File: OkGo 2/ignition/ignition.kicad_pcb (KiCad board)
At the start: 2 copper layers, 94 parts, among them K201 16A SPST, K202 16A SPST, K203 16A SPST, K204 16A SPST, K205 16A SPST, P105 BATT, P106 SMA, P107 ARM_LED, P201 CH3_LED, P203 CH3, P204 CH1_LED, P206 CH1, P207 CH4_LED, P209 CH4, P210 CH2_LED, P212 CH2, Q201 BSS138BK, Q202 BSS138BK, Q203 BSS138BK, Q204 BSS138BK, Q205 BSS138BK, U103 SWD, U105 RFM95W, U106 STM32F071CBT6, U107 TSR 0.5-2433, Y101 8MHz

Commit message: ignition; first attempt at placement
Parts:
- added REF**: hammond1555t2gy, ignition:hammond1555t2gy, F.Cu at (121.9, 101.0)
- added REF**: zippycompact-3s-5_8Ah, ignition:zippycompact-3s-5_8Ah-vert, F.Cu at (122.6, 120.0)
- P107, P201, P204, P207, P210: footprint common:JST-PA-2 -> ignition:JST-PA-2-VERT
- moved U107 221.8 mm to (48.3, 100.1), turned to 180 degrees
- moved R102 217.6 mm to (45.7, 79.2)
- moved R101 217.4 mm to (43.2, 79.2)
- moved TP101 208.6 mm to (43.2, 75.7)
- moved TP102 202.8 mm to (45.7, 75.7)
- moved R220 192.4 mm to (188.0, 76.2), turned to 180 degrees
- moved R218 191.2 mm to (188.0, 73.7), turned to 0 degrees
- moved Q204 189.9 mm to (188.0, 70.6), turned to 0 degrees
- moved D213 188.3 mm to (188.0, 67.1), turned to 0 degrees
- moved R216 179.9 mm to (193.5, 70.1)
- moved D212 178.1 mm to (193.5, 67.1), turned to 0 degrees
- moved R217 176.4 mm to (193.5, 72.6), turned to 0 degrees
- moved F101 172.5 mm to (76.7, 98.6), turned to 180 degrees
- moved TP206 170.2 mm to (193.5, 76.2)
- moved P207 167.4 mm to (166.6, 87.6)
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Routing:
- net /firing/FIRING_DIST: track 0.00 -> 84.6 mm
- net +BATT: track 0.00 -> 66.9 mm
- net Net-(D206-Pad1): track 0.00 -> 19.9 mm
- net Net-(D218-Pad1): track 0.00 -> 19.7 mm
- net Net-(D214-Pad1): track 0.00 -> 18.6 mm
- net Net-(D210-Pad1): track 0.00 -> 17.8 mm
- net Net-(D101-Pad1): track 0.00 -> 16.0 mm
- net (no net): track 0.00 -> 1.90 mm
- added copper zone on B.Cu, net GND
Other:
- board text removed: "ch1"
- board text removed: "ch2"
- board text removed: "ch3"
- board text removed: "ch4"
- board text removed: "upstream"

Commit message: ignition test routing somewhat done
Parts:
- moved TP104 60.7 mm to (49.3, 85.3)
- moved P107 11.2 mm to (46.0, 77.1)
- moved R103 11.2 mm to (50.5, 77.0)
- moved R101 9.71 mm to (44.2, 88.9)
- moved R102 9.71 mm to (46.7, 88.9)
- moved TP101 9.71 mm to (44.2, 85.3)
- moved TP102 9.71 mm to (46.7, 85.3)
- moved TP201 6.20 mm to (105.9, 81.8)
- moved C104 4.85 mm to (68.3, 77.7), turned to 0 degrees
- moved TP202 3.55 mm to (110.5, 81.5)
- moved TP203 3.33 mm to (113.3, 81.5)
- moved R208 2.54 mm to (153.4, 58.9), turned to 0 degrees
- moved R210 2.54 mm to (153.4, 61.5), turned to 180 degrees
- moved R223 2.54 mm to (148.3, 58.9), turned to 0 degrees
- moved R224 2.54 mm to (148.3, 61.5), turned to 180 degrees
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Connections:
- D217 pad 1: Net-(D217-Pad1) -> +BATT
- D217 pad 2: +BATT -> Net-(D217-Pad2)
- K205 pad 1: Net-(D217-Pad1) -> Net-(D217-Pad2)
- P210 pad 1: Net-(D217-Pad1) -> Net-(D217-Pad2)
- Q205 pad 3: Net-(D217-Pad1) -> Net-(D217-Pad2)
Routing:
- net +BATT: track 66.9 -> 337.7 mm
- net +3V3: track 0.00 -> 243.8 mm, vias 0 -> 4
- net GND: track 0.00 -> 100.1 mm, vias 0 -> 22
- net Net-(D213-Pad2): track 0.00 -> 52.8 mm
- net /SWDIO: track 0.00 -> 43.8 mm
- net /firing/UPSTREAM_RELAY: track 0.00 -> 27.2 mm
- net Net-(D218-Pad1): track 19.7 -> 45.7 mm
- net Net-(D210-Pad1): track 17.8 -> 43.4 mm
- net Net-(D214-Pad1): track 18.6 -> 42.5 mm
- net /SWDCLK: track 0.00 -> 23.2 mm
- net /firing/RELAY_SENSE: track 0.00 -> 20.9 mm
- net Net-(D201-Pad2): track 0.00 -> 18.9 mm
- net Net-(D206-Pad1): track 19.9 -> 38.6 mm
- net Net-(D217-Pad2): track 0.00 -> 17.5 mm
- net /nRST: track 0.00 -> 17.4 mm, vias 0 -> 2
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
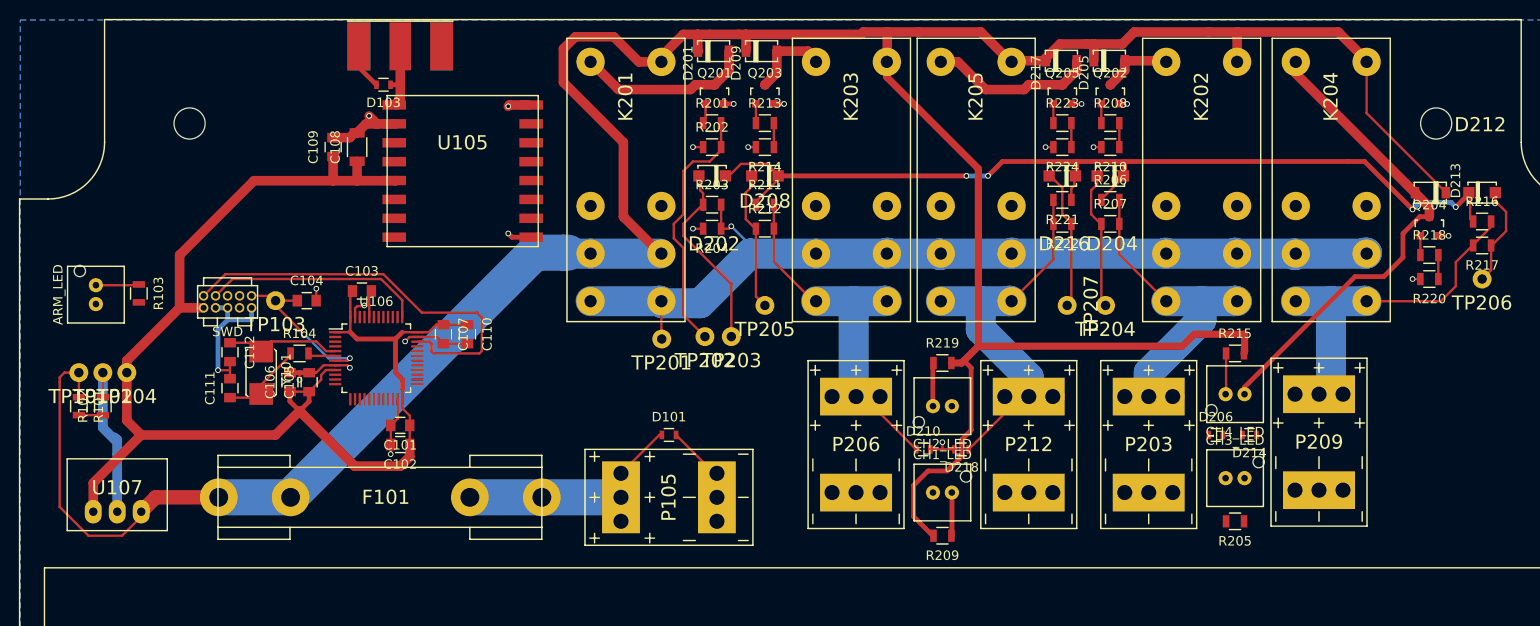
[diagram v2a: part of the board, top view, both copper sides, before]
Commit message: Provisional first place+pinassign+route of ignition
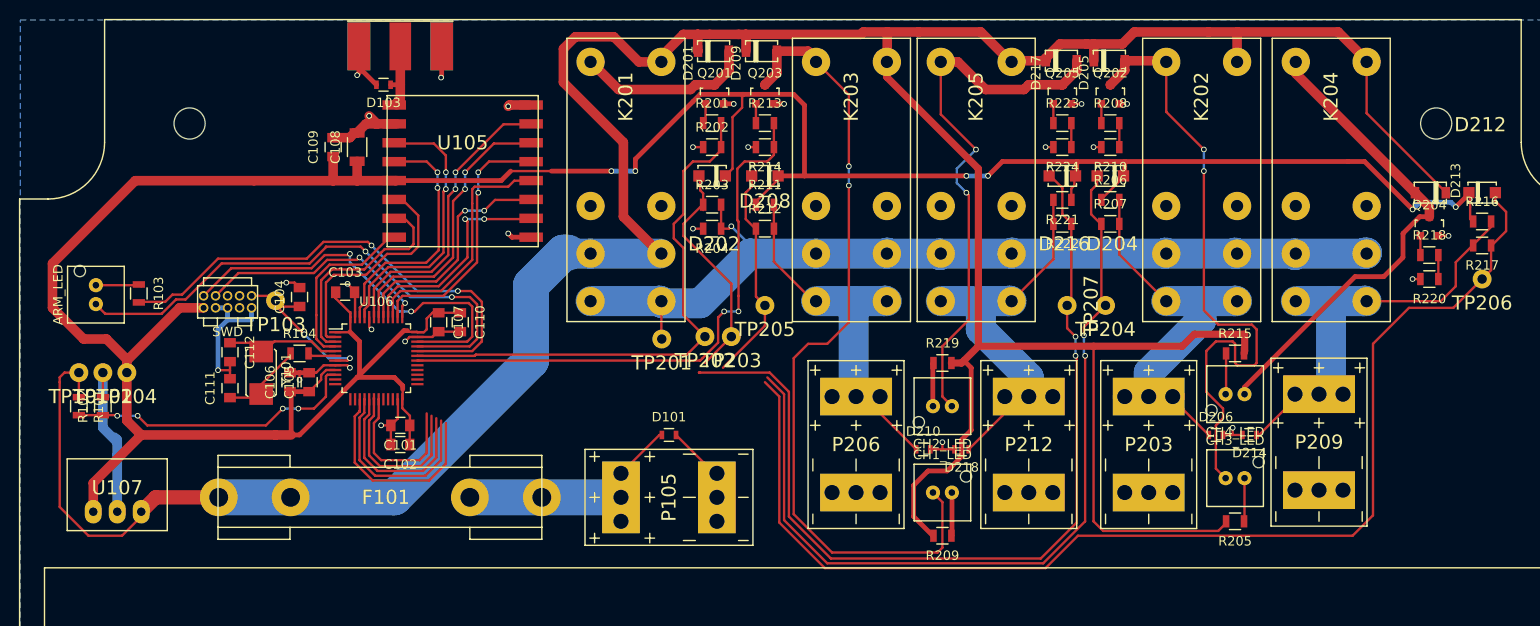
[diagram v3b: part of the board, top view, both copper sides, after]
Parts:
- moved C103 1.78 mm to (72.4, 76.8)
- moved C110 1.48 mm to (84.6, 80.0)
- moved C107 1.37 mm to (82.3, 80.0)
- moved C104 0.85 mm to (67.6, 77.3), turned to 90 degrees
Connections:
- P107 pad 1: (no net) -> /DISARM_LED
- R103 pad 2: (no net) -> /ARM_LED
- U105 pad 11: (no net) -> /RFM_DIO3
- U105 pad 12: (no net) -> /RFM_DIO4
- U105 pad 14: (no net) -> /RFM_DIO0
- U105 pad 15: (no net) -> /RFM_DIO1
- U105 pad 16: (no net) -> /RFM_DIO2
- U105 pad 2: (no net) -> /RFM_MISO
- U105 pad 3: (no net) -> /RFM_MOSI
- U105 pad 4: (no net) -> /RFM_SCK
- U105 pad 5: (no net) -> /RFM_NSS
- U105 pad 6: (no net) -> /RFM_RESET
- U105 pad 7: (no net) -> /RFM_DIO5
- U106 pad 10: (no net) -> /BATT_MON
- U106 pad 15: (no net) -> /firing/CONT_CH4
- U106 pad 16: (no net) -> /firing/CONT_CH3
- U106 pad 17: (no net) -> /firing/CONT_CH2
- U106 pad 18: (no net) -> /firing/CONT_CH1
- U106 pad 19: (no net) -> /firing/RELAY_SENSE
- U106 pad 2: (no net) -> /RFM_DIO0
- U106 pad 27: (no net) -> /firing/FIRE_CH4
- U106 pad 28: (no net) -> /firing/FIRE_CH3
- U106 pad 29: (no net) -> /firing/FIRE_CH2
- U106 pad 3: (no net) -> /RFM_DIO1
- U106 pad 30: (no net) -> /firing/FIRE_CH1
- U106 pad 31: (no net) -> /firing/UPSTREAM_RELAY
- U106 pad 32: (no net) -> /ARM_LED
- U106 pad 33: (no net) -> /DISARM_LED
- U106 pad 38: (no net) -> /RFM_NSS
- U106 pad 39: (no net) -> /RFM_SCK
- U106 pad 4: (no net) -> /RFM_DIO2
- U106 pad 40: (no net) -> /RFM_MISO
- U106 pad 41: (no net) -> /RFM_MOSI
- U106 pad 42: (no net) -> /RFM_RESET
- U106 pad 43: (no net) -> /RFM_DIO5
- U106 pad 45: (no net) -> /RFM_DIO3
- U106 pad 46: (no net) -> /RFM_DIO4
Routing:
- net /firing/CONT_CH4: track 10.7 -> 148.4 mm
- net /firing/CONT_CH2: track 15.2 -> 115.6 mm, vias 0 -> 2
- net /firing/CONT_CH3: track 15.3 -> 111.5 mm, vias 0 -> 2
- net +3V3: track 243.8 -> 324.5 mm, vias 4 -> 6
- net Net-(D209-Pad2): track 9.19 -> 86.1 mm, vias 0 -> 2
- net Net-(D205-Pad2): track 7.65 -> 68.6 mm, vias 0 -> 2
- net /firing/FIRE_CH1: track 2.63 -> 60.9 mm, vias 0 -> 2
- net /DISARM_LED: track 0.00 -> 56.7 mm, vias 0 -> 2
- net /ARM_LED: track 0.00 -> 53.1 mm, vias 0 -> 2
- net Net-(D217-Pad2): track 17.5 -> 58.5 mm, vias 0 -> 2
- net +BATT: track 337.7 -> 376.0 mm
- net /RFM_DIO5: track 0.00 -> 32.0 mm, vias 0 -> 2
- net /firing/UPSTREAM_RELAY: track 27.2 -> 58.5 mm
- net /RFM_RESET: track 0.00 -> 30.4 mm, vias 0 -> 2
- net /RFM_DIO3: track 0.00 -> 29.2 mm, vias 0 -> 2
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
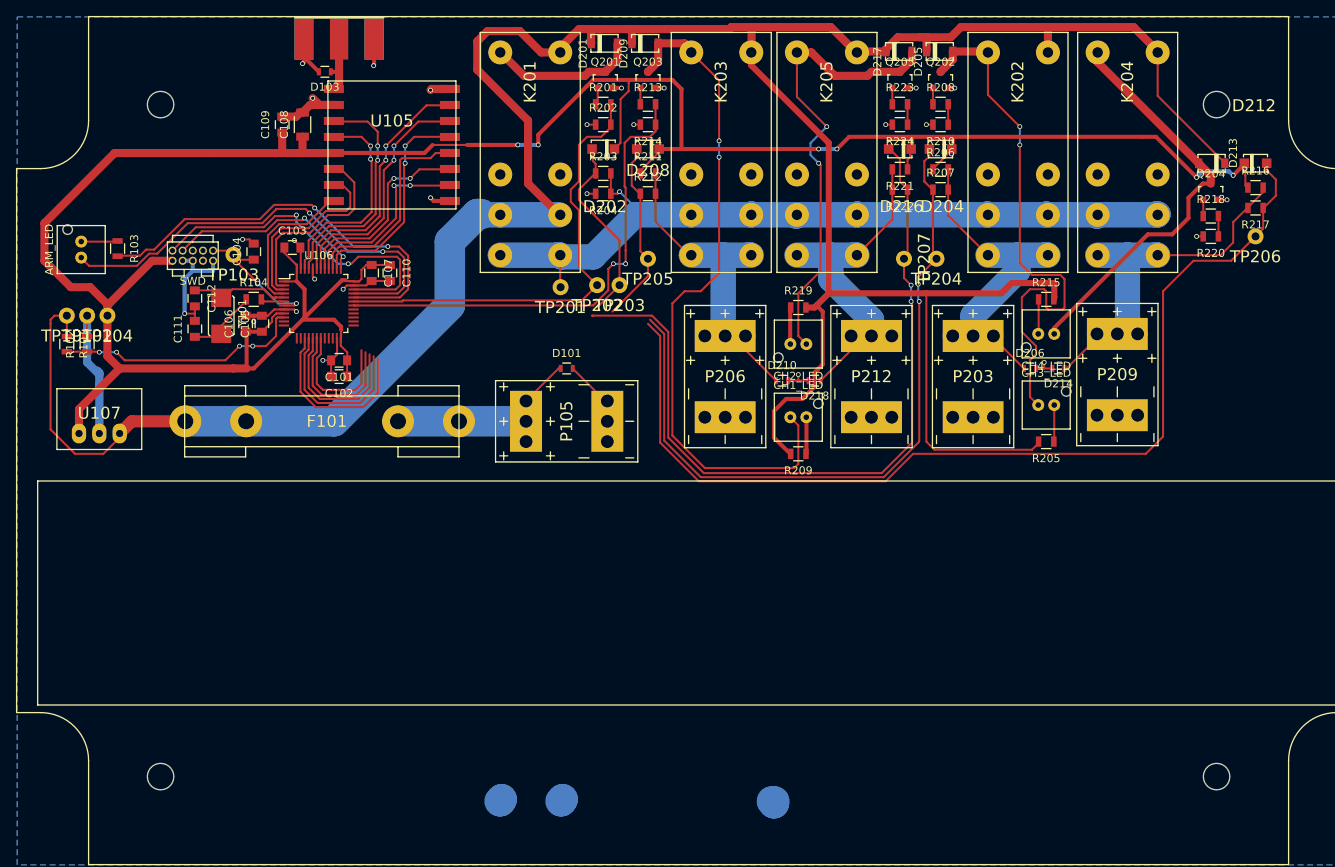
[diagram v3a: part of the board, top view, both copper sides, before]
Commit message: Second route of ignition
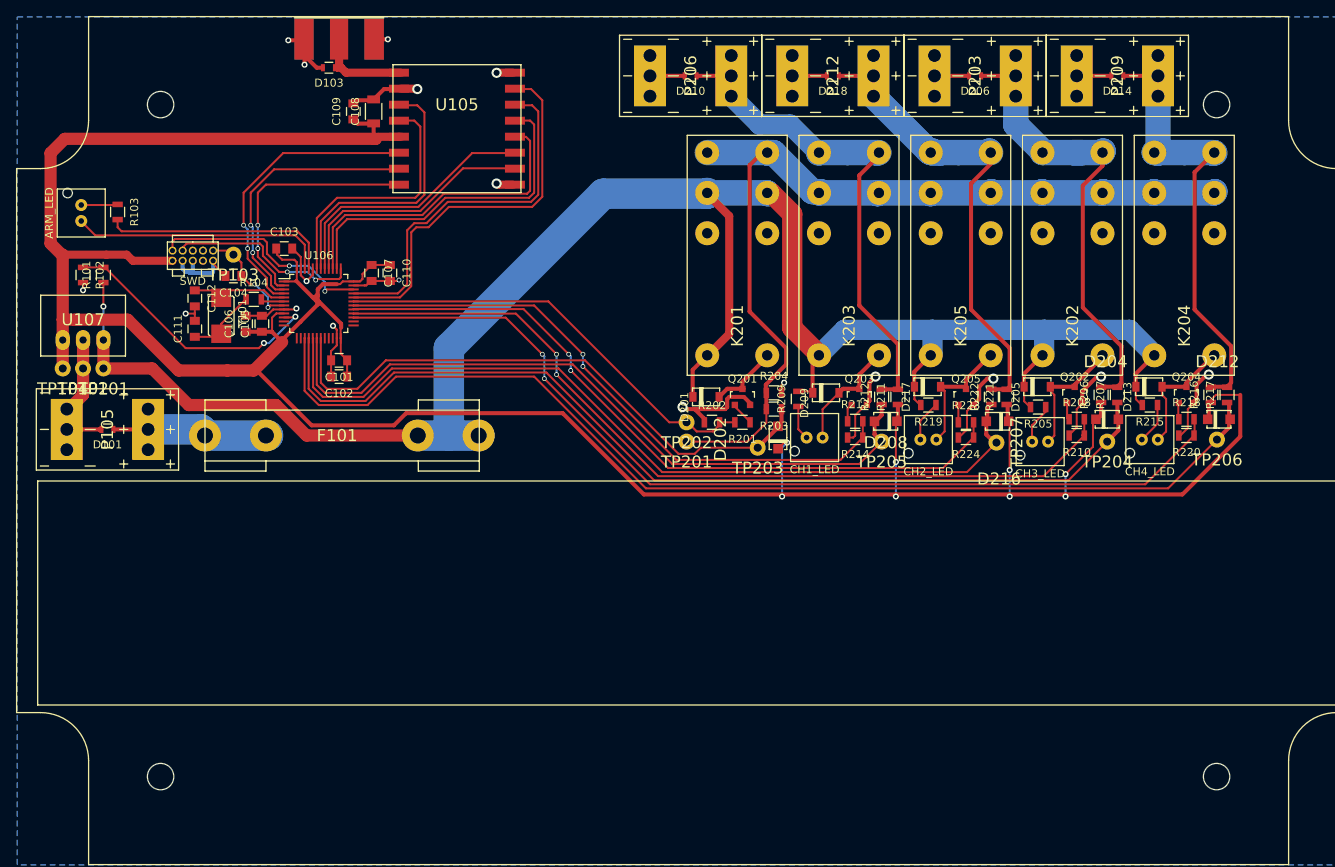
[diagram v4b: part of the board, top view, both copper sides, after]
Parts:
- moved D101 57.9 mm to (49.3, 99.6), turned to 180 degrees
- moved P105 57.4 mm to (49.3, 99.6), turned to 0 degrees
- moved D209 49.2 mm to (139.2, 95.0)
- moved Q203 47.6 mm to (143.3, 95.5)
- moved R213 47.3 mm to (142.7, 98.6)
- moved R214 46.9 mm to (142.7, 100.6)
- moved D201 46.0 mm to (124.2, 95.5)
- moved D208 45.2 mm to (146.6, 98.6)
- moved D205 43.6 mm to (165.6, 94.2)
- moved R201 43.4 mm to (128.7, 98.7), turned to 180 degrees
- moved Q201 43.2 mm to (128.7, 95.5)
- moved R208 42.9 mm to (170.4, 98.3)
- moved Q202 42.8 mm to (170.2, 95.2)
- moved R210 42.4 mm to (170.4, 100.3)
- moved D202 42.2 mm to (133.1, 100.6), turned to 270 degrees
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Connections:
- U106 pad 2: /RFM_DIO0 -> /RFM_DIO2
- U106 pad 32: /ARM_LED -> /RFM_DIO5
- U106 pad 33: /DISARM_LED -> /RFM_RESET
- U106 pad 4: /RFM_DIO2 -> /RFM_DIO0
- U106 pad 42: /RFM_RESET -> /RFM_DIO3
- U106 pad 43: /RFM_DIO5 -> /RFM_DIO4
- U106 pad 45: /RFM_DIO3 -> /ARM_LED
- U106 pad 46: /RFM_DIO4 -> /DISARM_LED
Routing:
- net +BATT: track 376.0 -> 255.6 mm, vias 0 -> 1
- net /firing/FIRE_CH4: track 2.63 -> 120.0 mm, vias 0 -> 2
- net /firing/FIRE_CH3: track 2.63 -> 105.7 mm, vias 0 -> 2
- net /firing/FIRE_CH2: track 2.63 -> 90.4 mm, vias 0 -> 2
- net Net-(D209-Pad2): track 86.1 -> 14.5 mm, vias 2 -> 0
- net Net-(D205-Pad2): track 68.6 -> 15.9 mm, vias 2 -> 0
- net /firing/CONT_CH1: track 41.5 -> 90.9 mm
- net +3V3: track 324.5 -> 368.1 mm, vias 6 -> 8
- net GND: track 108.6 -> 150.9 mm, vias 26 -> 18
- net Net-(D217-Pad2): track 58.5 -> 16.2 mm, vias 2 -> 0
- net Net-(D213-Pad2): track 52.8 -> 16.0 mm
- net /firing/RELAY_SENSE: track 41.2 -> 73.2 mm
- net /DISARM_LED: track 56.7 -> 32.2 mm, vias 2 -> 0
- net /ARM_LED: track 53.1 -> 28.9 mm, vias 2 -> 0
- net Net-(D210-Pad1): track 43.4 -> 66.9 mm
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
